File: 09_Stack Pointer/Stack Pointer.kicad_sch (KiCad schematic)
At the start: 4 parts, among them J1 Data bus, J2 Address bus 1, J3 Address bus 2, J4 Input 1

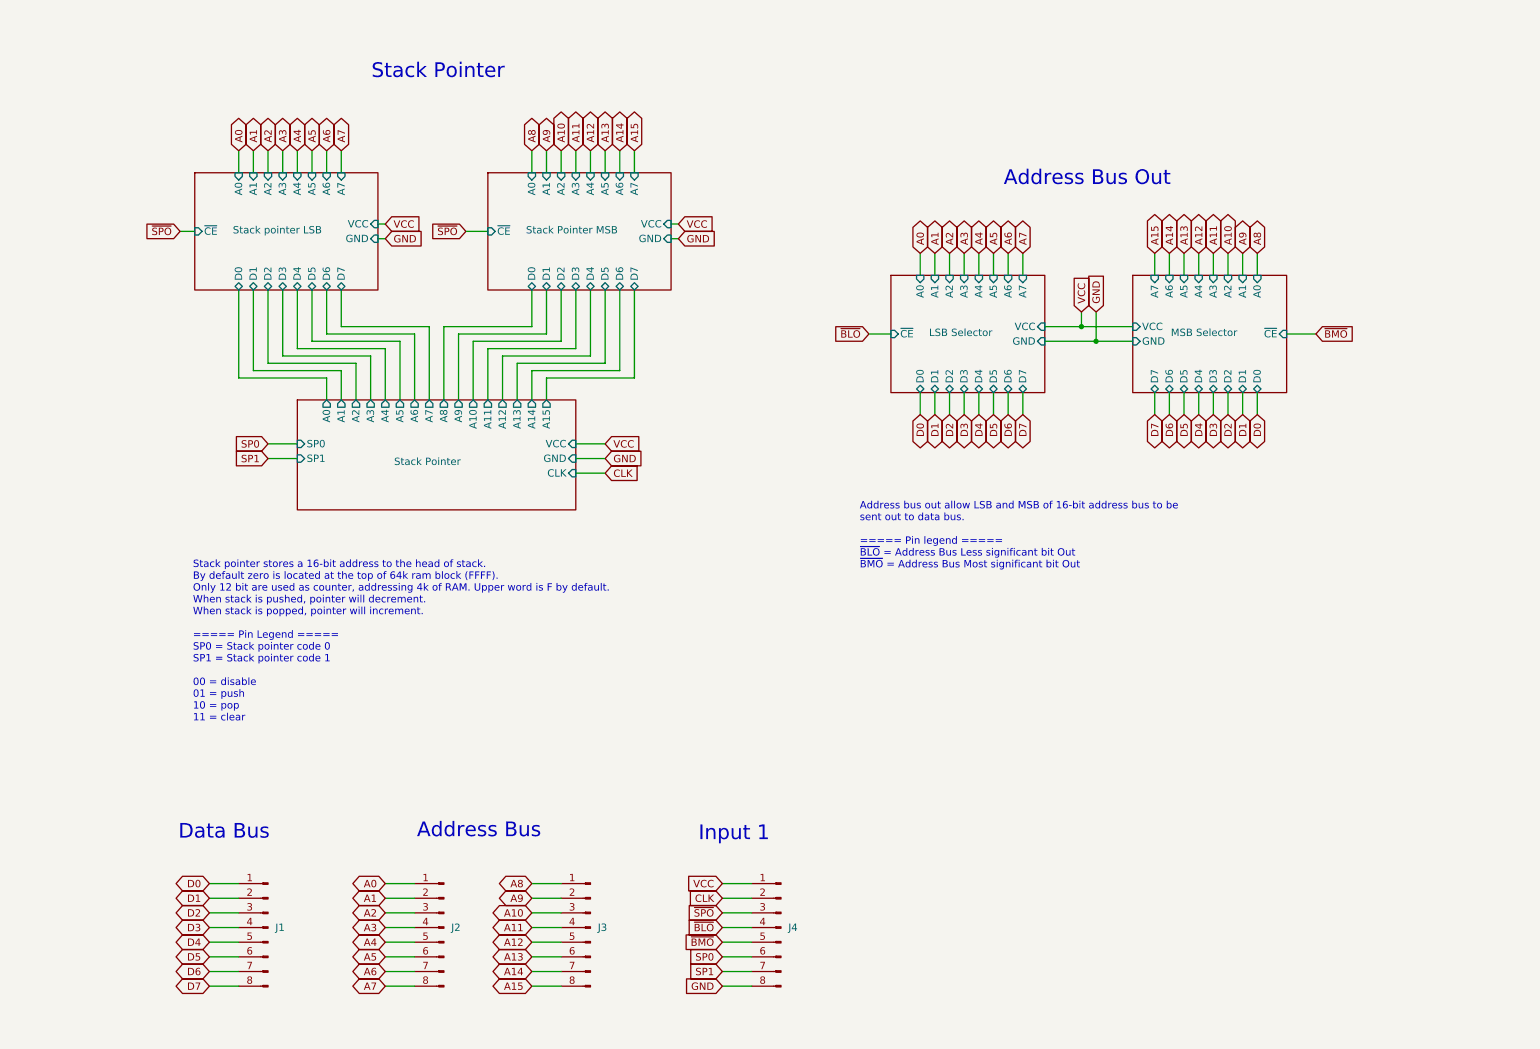
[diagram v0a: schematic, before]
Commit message: Last revision of the cpu, all boards have been ordered. Implementation to be tested and documented in following commits.
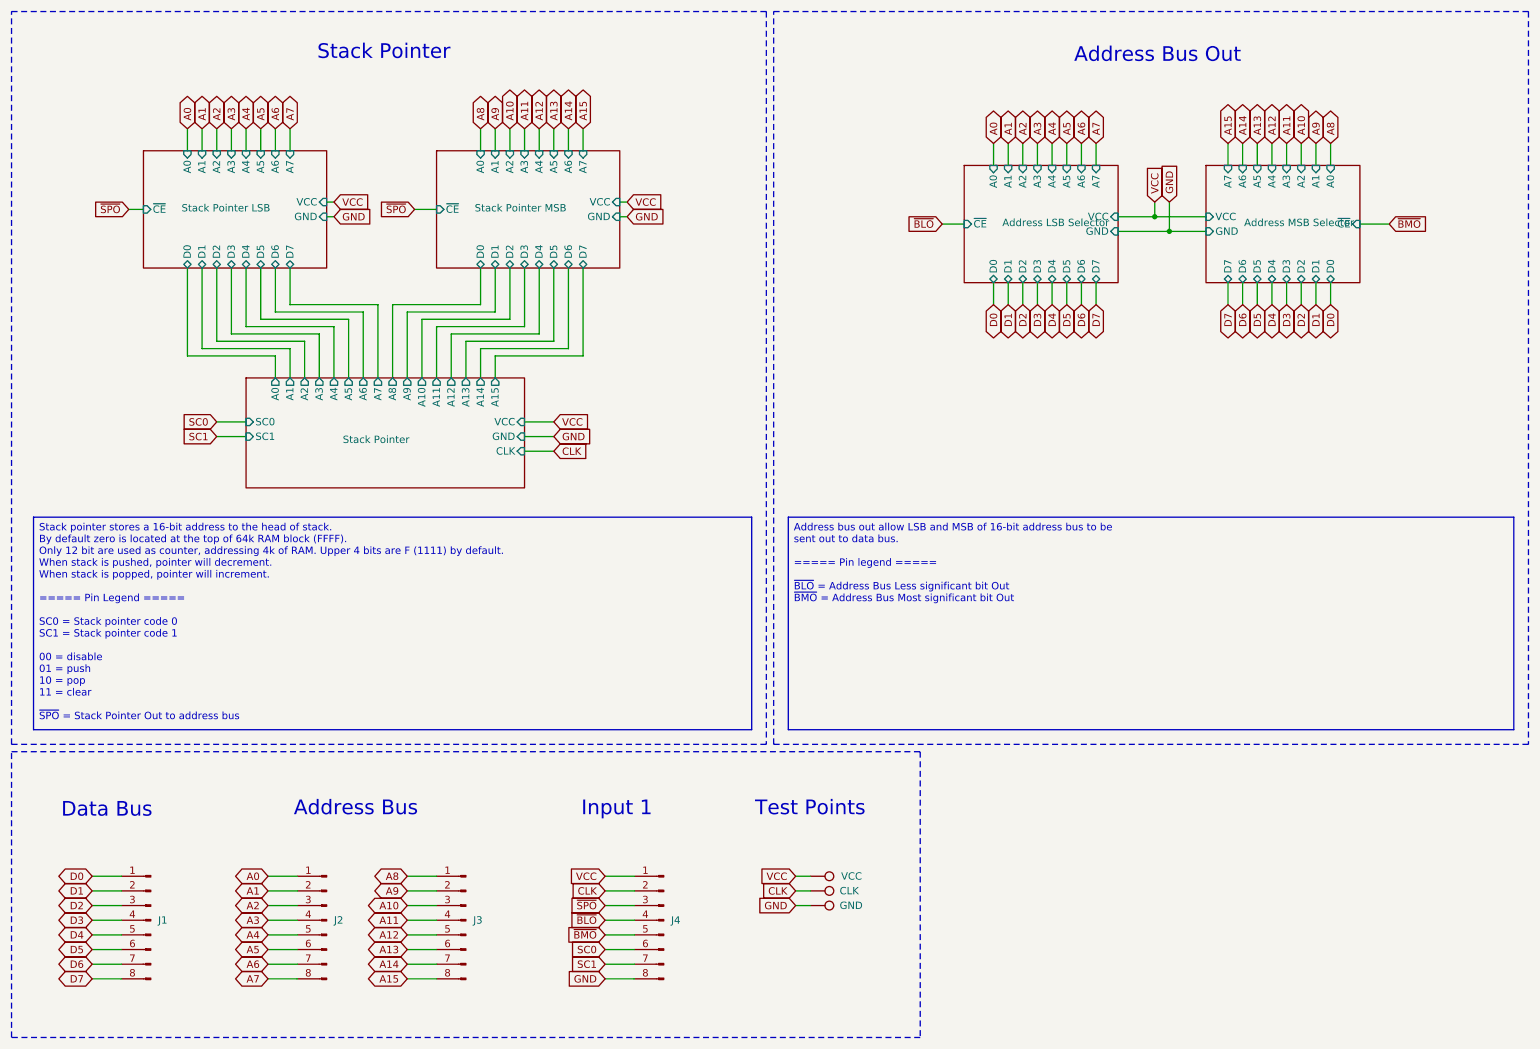
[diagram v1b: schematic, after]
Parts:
- added TP1: VCC, TestPoint:TestPoint_Loop_D3.50mm_Drill0.9mm_Beaded, symbol Connector:TestPoint
- added TP2: CLK, TestPoint:TestPoint_Loop_D3.50mm_Drill0.9mm_Beaded, symbol Connector:TestPoint
- added TP3: GND, TestPoint:TestPoint_Loop_D3.50mm_Drill0.9mm_Beaded, symbol Connector:TestPoint
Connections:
- net CLK: now also TP2.1
- net GND: now also TP3.1
- net VCC: now also TP1.1
- net SP0 renamed SC0
- net SP1 renamed SC1
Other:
- sheet LSB Selector renamed Address LSB Selector
- sheet MSB Selector renamed Address MSB Selector
- sheet Stack pointer LSB renamed Stack Pointer LSB
- sheet Stack Pointer ports: added SC0, SC1; removed SP0, SP1
- note added: "Test Points"
- moved on the sheet: J1, J2, J3, J4
